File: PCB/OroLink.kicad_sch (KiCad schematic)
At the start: 11 parts, among them J1 67996-408HLF

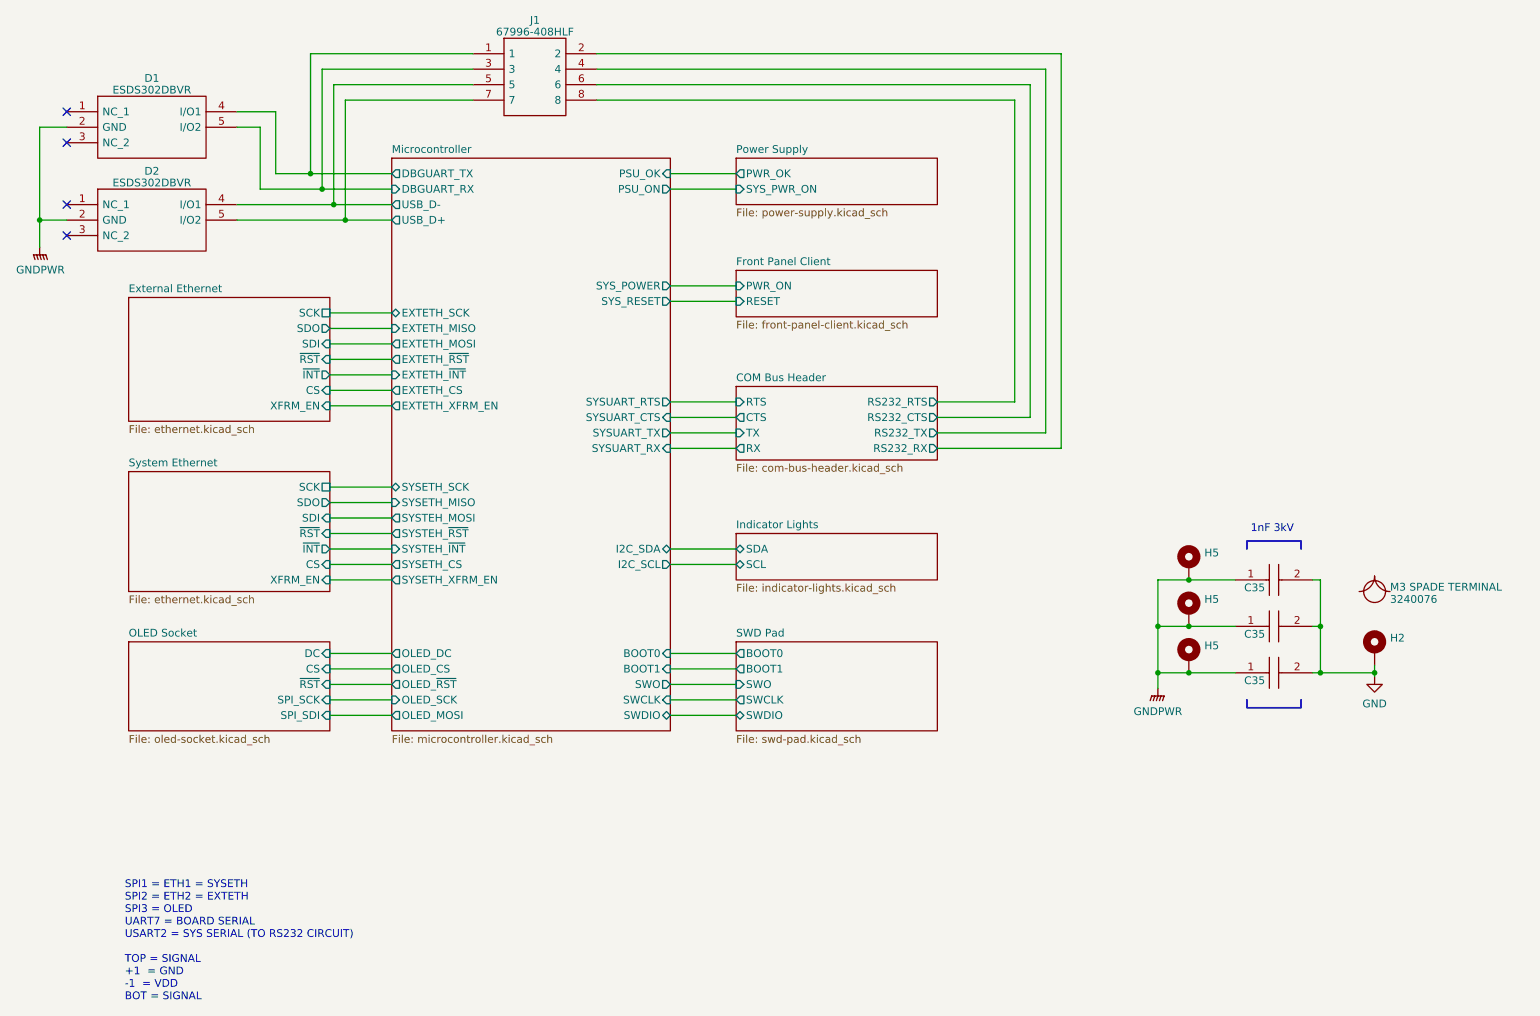
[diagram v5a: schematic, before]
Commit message: ethernet ports wired up
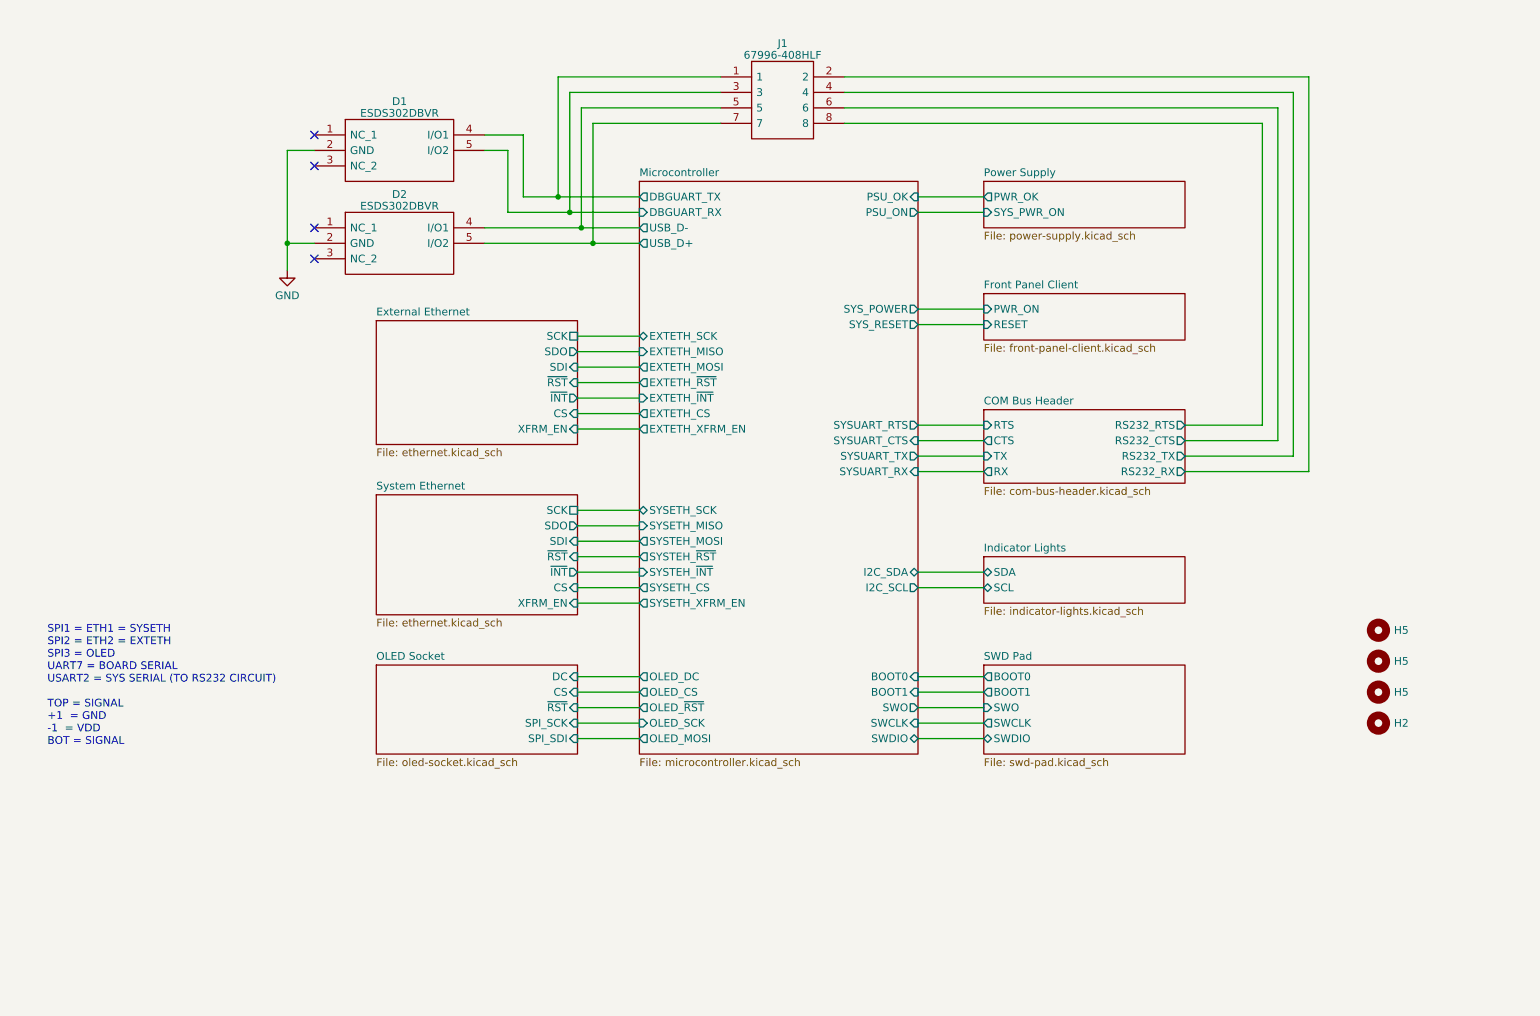
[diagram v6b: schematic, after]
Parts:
- removed B2: 3240076, symbol Oro:BOM Part
- removed C35 (x3): 1nF 5kV, CAPC4620X220N, symbol SamacSys_Parts:885342210004
- H2, H5: symbol Mechanical:MountingHole_Pad -> Mechanical:MountingHole; now in the parts list
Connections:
- net GND: now also D1.2 (GND), D2.2 (GND); no longer H2.1
- removed net GNDPWR: D1.2 (GND), D2.2 (GND), H5.1, H5.1, H5.1
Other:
- note removed: "1nF 3kV"
- moved on the sheet: D1, D2, J1

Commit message: rs232 and usb lines wired up
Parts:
- D1, D2: symbol SamacSys_Parts:ESDS302DBVR -> Oro:ESDS302DBVR_tied
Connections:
- net COM Bus Header/RS232_RX: now also J1.4; no longer J1.2
- net COM Bus Header/RS232_TX: now also J1.2; no longer J1.4
- net Microcontroller/DBGUART_RX: now also D1.1 (NC_1)
- net Microcontroller/DBGUART_TX: now also D1.3 (NC_2)
- net Microcontroller/USB_D+: now also D2.1 (NC_1)
- net Microcontroller/USB_D-: now also D2.3 (NC_2)
- no-connect marks 4 -> 0
